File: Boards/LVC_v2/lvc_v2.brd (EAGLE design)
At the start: 17 parts, among them U1 LMR16020

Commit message: routed lightAPRS LVC
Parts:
- removed U$2: LITEAPRS, NR_connectors:LITEAPRS
- added JP3: (no value), pinhead:1X01
- moved C4 3.15 mm to (10.4, 26.9), turned to 180 degrees
- moved C3 2.26 mm to (23.6, 16.1)
- moved R21 2.18 mm to (24.9, 22.8), turned to 270 degrees
- moved C5 2.03 mm to (20.2, 16.1)
- moved C2 1.74 mm to (16.3, 18.2), turned to 0 degrees
- moved C11 1.48 mm to (10.3, 29.1)
- moved D3 1.42 mm to (12.0, 18.4), turned to 0 degrees
- moved R19 0.80 mm to (19.0, 27.4)
- moved L1 0.76 mm to (11.4, 23.0)
- moved R17 0.76 mm to (22.1, 27.6)
- moved R20 0.76 mm to (24.9, 27.6)
- moved U$1 0.76 mm to (37.6, 19.1)
- moved U$3 0.76 mm to (30.8, 29.0)
- moved U1 0.76 mm to (19.3, 23.1)
- moved R18 0.45 mm to (15.3, 27.3), turned to 180 degrees
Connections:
- net GND: now also JP3.1; no longer U$2.P$2
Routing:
- net SW: track 0.00 -> 11.2 mm
- net N$7: track 0.00 -> 8.28 mm
- net N$31: track 0.00 -> 6.20 mm
- net FB: track 0.00 -> 4.47 mm
- net IN1: track 0.00 -> 2.93 mm
- net N$29: track 0.00 -> 1.78 mm
- added copper zone on layer 1, net +3V3
- added copper zone on layer 1, net IN1
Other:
- board outline added: 24.8 x 23 mm
- board text added: "</CMD>"
- board text added: "GND"
- board text added: "^3V3"

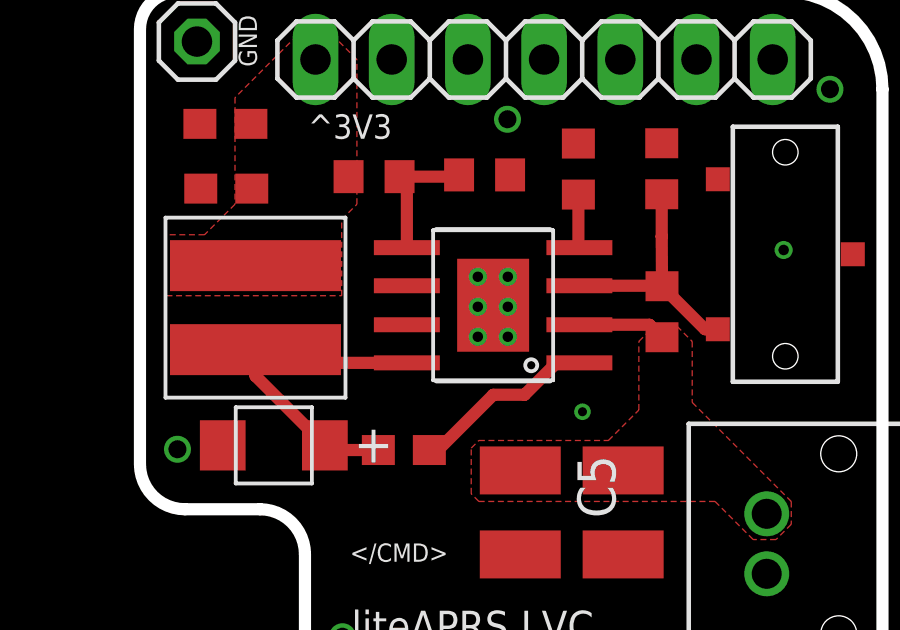
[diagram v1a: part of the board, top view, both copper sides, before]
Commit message: Cutting down the adafruit rfm board
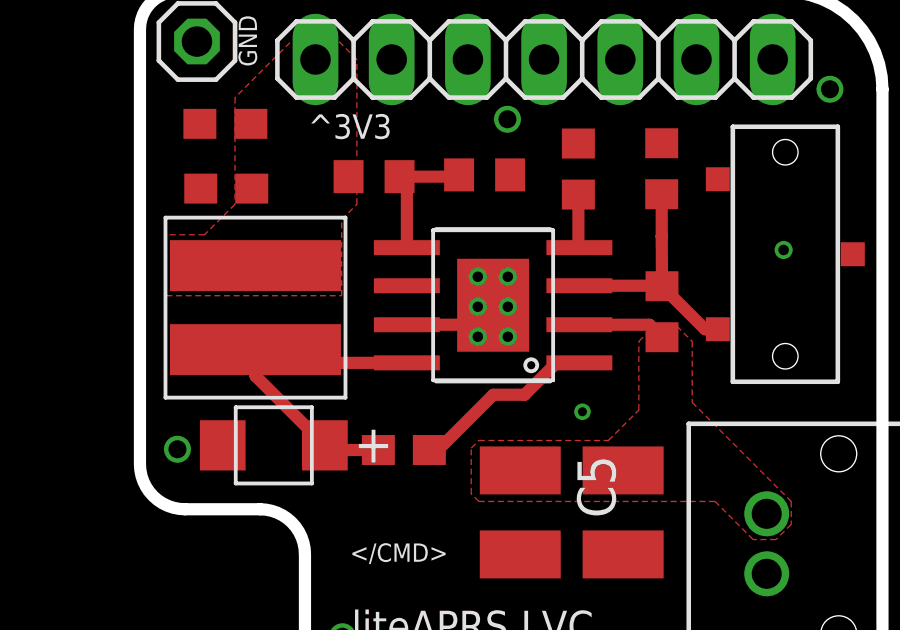
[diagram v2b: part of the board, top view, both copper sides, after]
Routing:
- net GND: track 0.00 -> 3.14 mm
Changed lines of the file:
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@@
 <setting verticaltext="up"/>
 </settings>
-<grid distance="0.25" unitdist="mm" unit="mm" style="lines" multiple="4" display="yes" altdistance="0.1" altunitdist="mm" altunit="mm"/>
+<grid distance="0.25" unitdist="mm" unit="mm" style="lines" multiple="1" display="yes" altdistance="0.1" altunitdist="mm" altunit="mm"/>
 <layers>
 <layer number="1" name="Top" color="4" fill="1" visible="yes" active="yes"/>
@@
 <layer number="46" name="Milling" color="3" fill="1" visible="no" active="yes"/>
 <layer number="47" name="Measures" color="7" fill="1" visible="no" active="yes"/>
-<layer number="48" name="Document" color="7" fill="1" visible="no" active="yes"/>
+<layer number="48" name="Document" color="7" fill="1" visible="yes" active="yes"/>
 <layer number="49" name="Reference" color="7" fill="1" visible="no" active="yes"/>
 <layer number="50" name="dxf" color="7" fill="1" visible="no" active="no"/>
@@
 <text x="11.4" y="31" size="0.6096" layer="21" rot="R90">GND</text>
 <text x="14.5" y="14.5" size="0.6096" layer="21">&lt;/CMD&gt;</text>
+<dimension x1="7.25" y1="38.25" x2="32.75" y2="38.25" x3="20" y3="39.75" textsize="1.778" layer="48"/>
+<dimension x1="36.5" y1="33.75" x2="36.5" y2="10.25" x3="48" y3="22" textsize="1.778" layer="48"/>
 </plain>
 <attributes>
@@
 <via x="22.25" y="19.5" extent="1-16" drill="0.3"/>
 <via x="19.75" y="29.25" extent="1-16" drill="0.6"/>
-<wire x1="16.397" y1="22.4" x2="18.762" y2="22" width="0" layer="19" extent="1-1"/>
+<wire x1="16.397" y1="22.4" x2="18.622" y2="22.4" width="0.4064" layer="1"/>
+<wire x1="18.622" y1="22.4" x2="19.272" y2="23.05" width="0.4064" layer="1"/>
 </signal>
 <signal name="N$2">
@@
 <vertex x="18.796" y="18.542"/>
 <vertex x="23.114" y="18.542"/>
-<vertex x="23.114" y="18.542"/>
 <vertex x="24.13" y="19.558"/>

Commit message: Box changes
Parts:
- moved U$1 0.75 mm to (37.6, 19.8)
- moved D3 0.50 mm to (12.0, 17.9)
- moved C4 0.20 mm to (10.4, 27.1)
- moved C11 0.10 mm to (10.3, 29.2)
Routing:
- net SW: track 11.2 -> 11.8 mm
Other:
- board text added: "VIN 2S Li"
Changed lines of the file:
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@@
 <wire x1="7.5" y1="17.75" x2="7.5" y2="32.25" width="0.4064" layer="20"/>
 <wire x1="7.5" y1="32.25" x2="8.75" y2="33.5" width="0.4064" layer="20" curve="-90"/>
-<text x="14.55" y="11.85" size="1.016" layer="21" font="vector">liteAPRS LVC</text>
+<text x="14.8" y="12.35" size="1.016" layer="21" font="vector">liteAPRS LVC</text>
 <text x="13.1" y="28.6" size="0.8128" layer="21">^3V3</text>
 <text x="11.4" y="31" size="0.6096" layer="21" rot="R90">GND</text>
-<text x="14.5" y="14.5" size="0.6096" layer="21">&lt;/CMD&gt;</text>
+<text x="18.25" y="19.25" size="0.6096" layer="21">&lt;/CMD&gt;</text>
 <dimension x1="7.25" y1="38.25" x2="32.75" y2="38.25" x3="20" y3="39.75" textsize="1.778" layer="48"/>
 <dimension x1="36.5" y1="33.75" x2="36.5" y2="10.25" x3="48" y3="22" textsize="1.778" layer="48"/>
+<text x="13.75" y="15.75" size="0.6096" layer="21">VIN 2S Li</text>
+<text x="13.75" y="14.25" size="0.6096" layer="21">GND</text>
 </plain>
 <attributes>
@@
 <attribute name="VALUE" x="20.431" y="18.049" size="1.27" layer="27" rot="R270"/>
 </element>
-<element name="C4" library="resistor" package="C0603" value=".18 uF" x="10.377375" y="26.93825" smashed="yes" rot="R180">
-<attribute name="VALUE" x="11.012375" y="28.84325" size="1.27" layer="27" rot="R180"/>
+<element name="C4" library="resistor" package="C0603" value=".18 uF" x="10.377375" y="27.13825" smashed="yes" rot="R180">
+<attribute name="VALUE" x="11.012375" y="29.04325" size="1.27" layer="27" rot="R180"/>
 </element>
 <element name="C5" library="resistor" package="C1210" value="2.2 uF" x="20.177" y="16.144" smashed="yes" rot="R270">
@@
 <attribute name="VALUE" x="17.002" y="18.049" size="1.27" layer="27" rot="R270"/>
 </element>
-<element name="C11" library="resistor" package="C0603" value="10 uF" x="10.346625" y="29.09625" smashed="yes" rot="R180">
-<attribute name="VALUE" x="10.981625" y="31.00125" size="1.27" layer="27" rot="R180"/>
+<element name="C11" library="resistor" package="C0603" value="10 uF" x="10.346625" y="29.19625" smashed="yes" rot="R180">
+<attribute name="VALUE" x="10.981625" y="31.10125" size="1.27" layer="27" rot="R180"/>
 </element>
 <element name="U1" library="HASP" package="SO8" value="LMR16020" x="19.272" y="23.05" smashed="yes" rot="R90">
 <attribute name="VALUE" x="24.987" y="18.605" size="1.27" layer="27" rot="R90"/>
 </element>
-<element name="D3" library="HASP" package="DO-214AC" value="DO-214AC" x="11.961375" y="18.379375" smashed="yes">
-<attribute name="VALUE" x="8.786375" y="15.204375" size="1.27" layer="27"/>
+<element name="D3" library="HASP" package="DO-214AC" value="DO-214AC" x="11.961375" y="17.879375" smashed="yes">
+<attribute name="VALUE" x="8.786375" y="14.704375" size="1.27" layer="27"/>
 </element>
 <element name="R20" library="resistor" package="R0603" value="30.1k" x="24.891375" y="27.600375" smashed="yes" rot="R270">
@@
 <attribute name="VALUE" x="22.9964" y="23.468975" size="1.27" layer="27" rot="R270"/>
 </element>
-<element name="U$1" library="jmolterLib" package="559350210" value="559350210" x="37.592" y="19.098" smashed="yes" rot="R270"/>
+<element name="U$1" library="jmolterLib" package="559350210" value="559350210" x="37.592" y="19.848" smashed="yes" rot="R270"/>
 <element name="U$3" library="jmolterLib" package="CL-SB-12B-01" value="CL-SB-12B-01" x="30.762" y="29" smashed="yes" rot="R270"/>
 <element name="JP3" library="pinhead" library_urn="urn:adsk.eagle:library:325" package="1X01" package3d_urn="urn:adsk.eagle:package:22485/2" value="" x="9.4" y="31.84" smashed="yes">
@@
 <via x="28.956" y="24.892" extent="1-16" drill="0.35"/>
 <contactref element="JP3" pad="1"/>
-<via x="14.25" y="12" extent="1-16" drill="0.6"/>
+<via x="14.5" y="13" extent="1-16" drill="0.6"/>
 <via x="8.75" y="18.25" extent="1-16" drill="0.6"/>
 <via x="30.5" y="30.25" extent="1-16" drill="0.6"/>
@@
 <contactref element="D3" pad="P$2"/>
 <contactref element="C2" pad="1"/>
-<wire x1="13.663175" y1="18.379375" x2="11.35075" y2="20.6918" width="0.4064" layer="1"/>
-<wire x1="11.35075" y1="20.6918" x2="11.35075" y2="21.570625" width="0.4064" layer="1"/>
+<wire x1="13.663175" y1="17.879375" x2="11.35075" y2="20.1918" width="0.4064" layer="1"/>
+<wire x1="11.35075" y1="20.1918" x2="11.35075" y2="21.570625" width="0.4064" layer="1"/>
 <wire x1="16.397" y1="21.13" x2="11.791375" y2="21.13" width="0.4064" layer="1"/>
 <wire x1="11.791375" y1="21.13" x2="11.35075" y2="21.570625" width="0.4064" layer="1"/>
-<wire x1="13.663175" y1="18.379375" x2="13.818675" y2="18.223875" width="0.4064" layer="1" curve="90"/>
-<wire x1="13.818675" y1="18.223875" x2="15.446" y2="18.223875" width="0.4064" layer="1"/>
+<wire x1="13.663175" y1="17.879375" x2="14.007675" y2="18.223875" width="0.4064" layer="1" curve="90"/>
+<wire x1="14.007675" y1="18.223875" x2="15.446" y2="18.223875" width="0.4064" layer="1"/>
 </signal>
 <signal name="FB">
@@
 <wire x1="24.485375" y1="22.4" x2="22.147" y2="22.4" width="0.4064" layer="1"/>
 <polygon width="0.4064" layer="1">
-<vertex x="28.702" y="15.24"/>
-<vertex x="27.94" y="15.24"/>
+<vertex x="29.202" y="15.99"/>
+<vertex x="27.19" y="15.99"/>
 <vertex x="26.67" y="16.51"/>
 <vertex x="18.796" y="16.51"/>
@@
 <vertex x="25.4" y="22.352"/>
 <vertex x="25.908" y="21.844"/>
-<vertex x="25.908" y="19.812"/>
-<vertex x="29.21" y="16.51"/>
-<vertex x="29.21" y="15.748"/>
+<vertex x="25.908" y="20.562"/>
+<vertex x="29.202" y="17.268"/>
 </polygon>
 </signal>

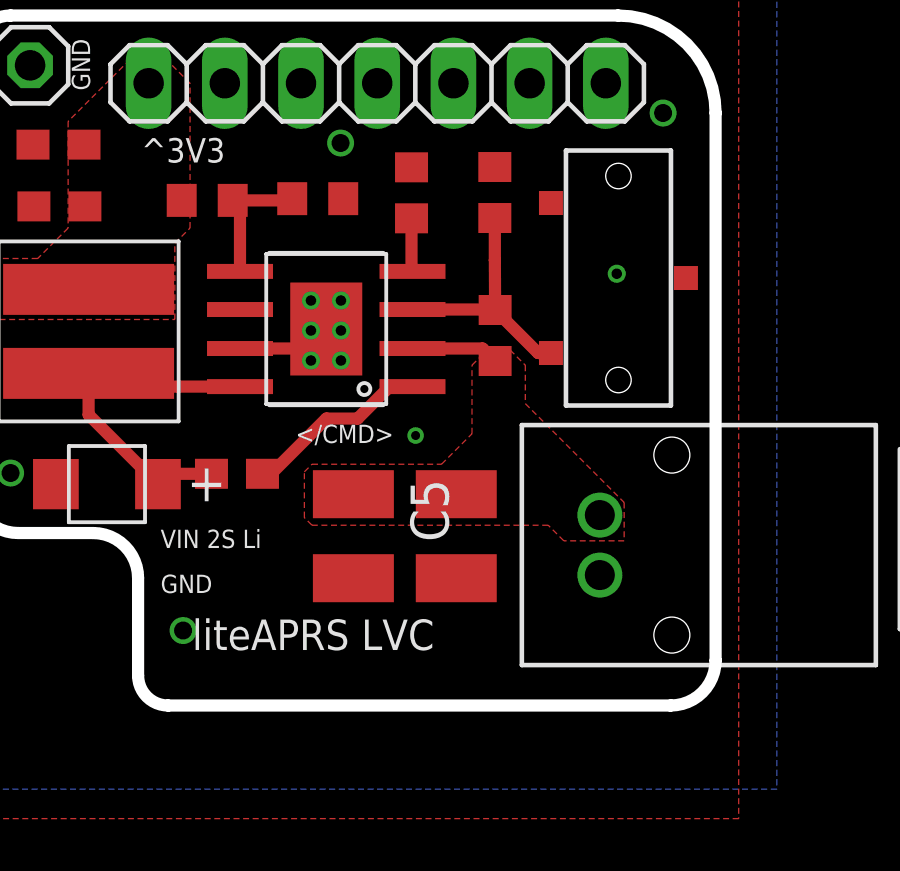
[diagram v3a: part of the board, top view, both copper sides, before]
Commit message: re-order/confirm LVC fix
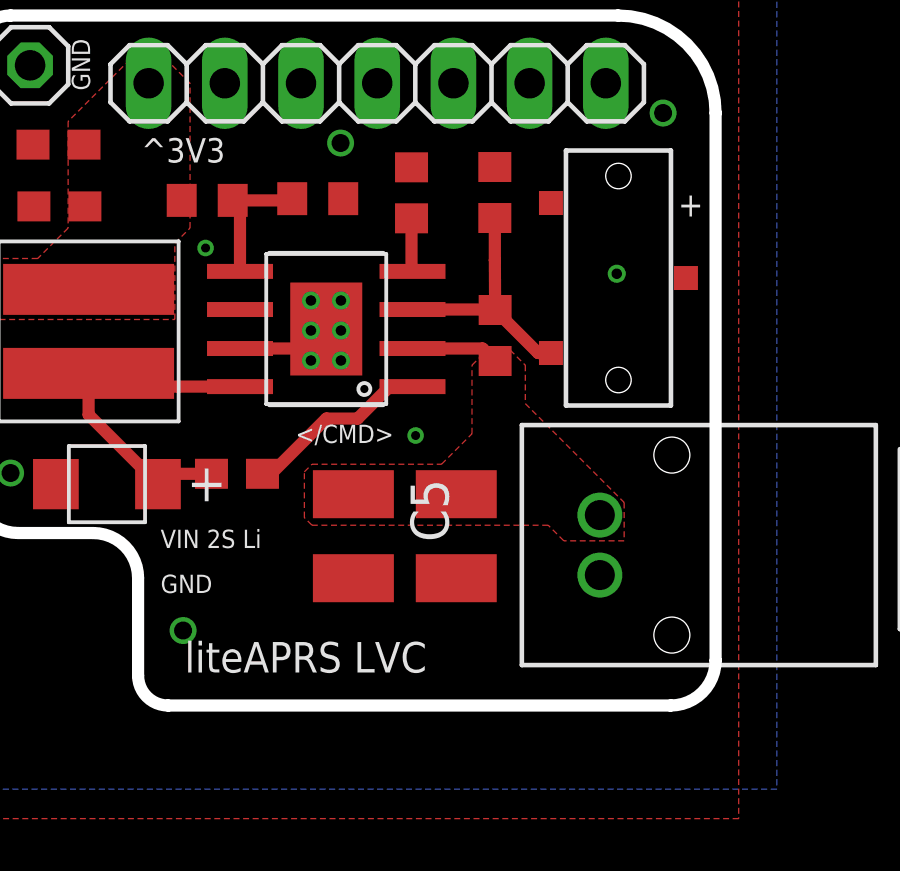
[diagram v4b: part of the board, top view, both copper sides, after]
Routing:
- net GND: vias 12 -> 13
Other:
- board text added: "+"
- board text added: "3v3 buck reg 2s LiPo Input Builtin LVC"
- board text added: "<GND"
- board text added: "<VIN"
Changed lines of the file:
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@@
 <wire x1="7.5" y1="17.75" x2="7.5" y2="32.25" width="0.4064" layer="20"/>
 <wire x1="7.5" y1="32.25" x2="8.75" y2="33.5" width="0.4064" layer="20" curve="-90"/>
-<text x="14.8" y="12.35" size="1.016" layer="21" font="vector">liteAPRS LVC</text>
+<text x="14.55" y="11.6" size="1.016" layer="21" font="vector">liteAPRS LVC</text>
 <text x="13.1" y="28.6" size="0.8128" layer="21">^3V3</text>
 <text x="11.4" y="31" size="0.6096" layer="21" rot="R90">GND</text>
@@
 <text x="13.75" y="15.75" size="0.6096" layer="21">VIN 2S Li</text>
 <text x="13.75" y="14.25" size="0.6096" layer="21">GND</text>
+<text x="27.3" y="16.3" size="0.8128" layer="22" rot="MR0">&lt;VIN</text>
+<text x="27.4" y="14.4" size="0.8128" layer="22" rot="MR0">&lt;GND</text>
+<text x="17.5" y="26" size="0.8128" layer="22" rot="MR0">3v3 buck reg
+2s LiPo Input
+Builtin LVC</text>
+<text x="31" y="26.8" size="0.8128" layer="21">+</text>
 </plain>
 <attributes>
@@
 <wire x1="16.397" y1="22.4" x2="18.622" y2="22.4" width="0.4064" layer="1"/>
 <wire x1="18.622" y1="22.4" x2="19.272" y2="23.05" width="0.4064" layer="1"/>
+<via x="15.25" y="25.75" extent="1-16" drill="0.3"/>
 </signal>
 <signal name="N$2">
